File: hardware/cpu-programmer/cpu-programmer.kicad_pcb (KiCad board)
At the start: 2 copper layers, 58 x 22 mm, 13 parts, among them J1 Conn_01x15_Socket, J2 Conn_01x04_Socket, SW1 SW_Push, SW2 SW_Push

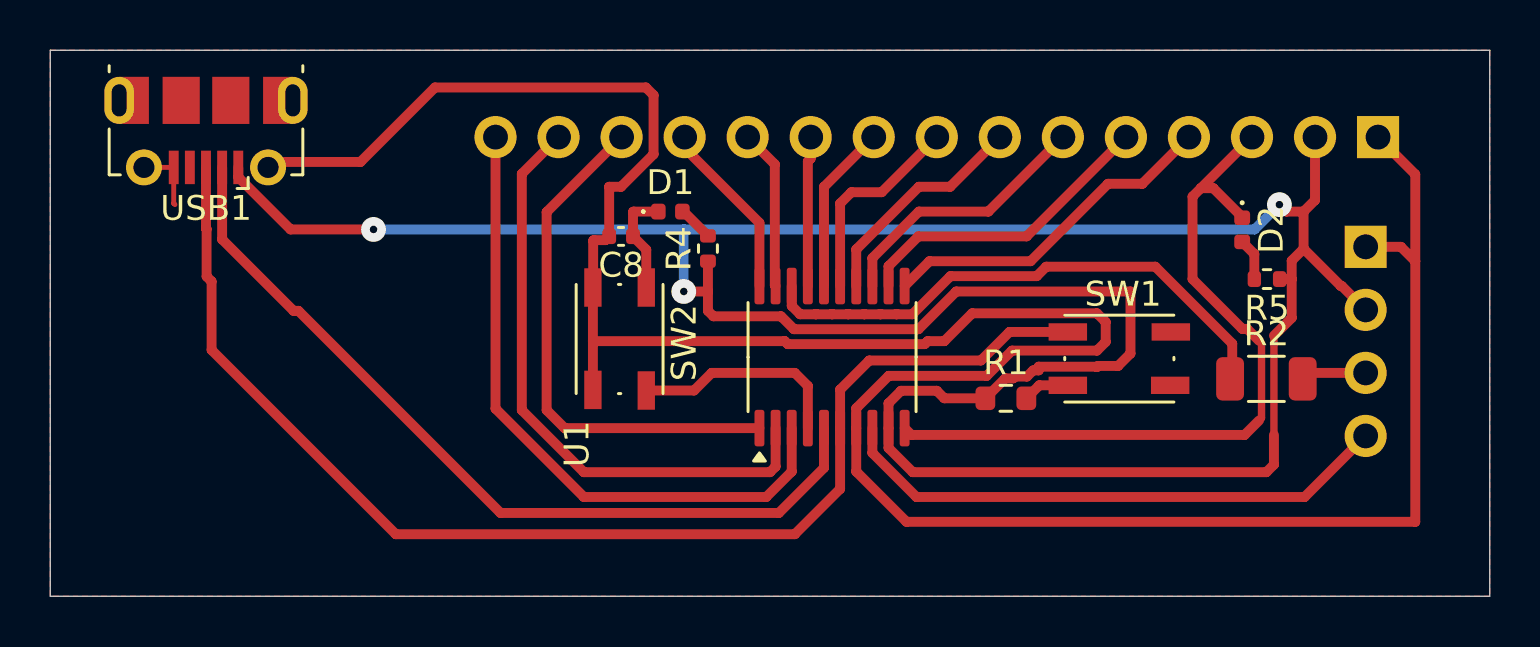
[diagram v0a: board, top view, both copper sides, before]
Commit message: Updated PCB, parts use at least package 0603
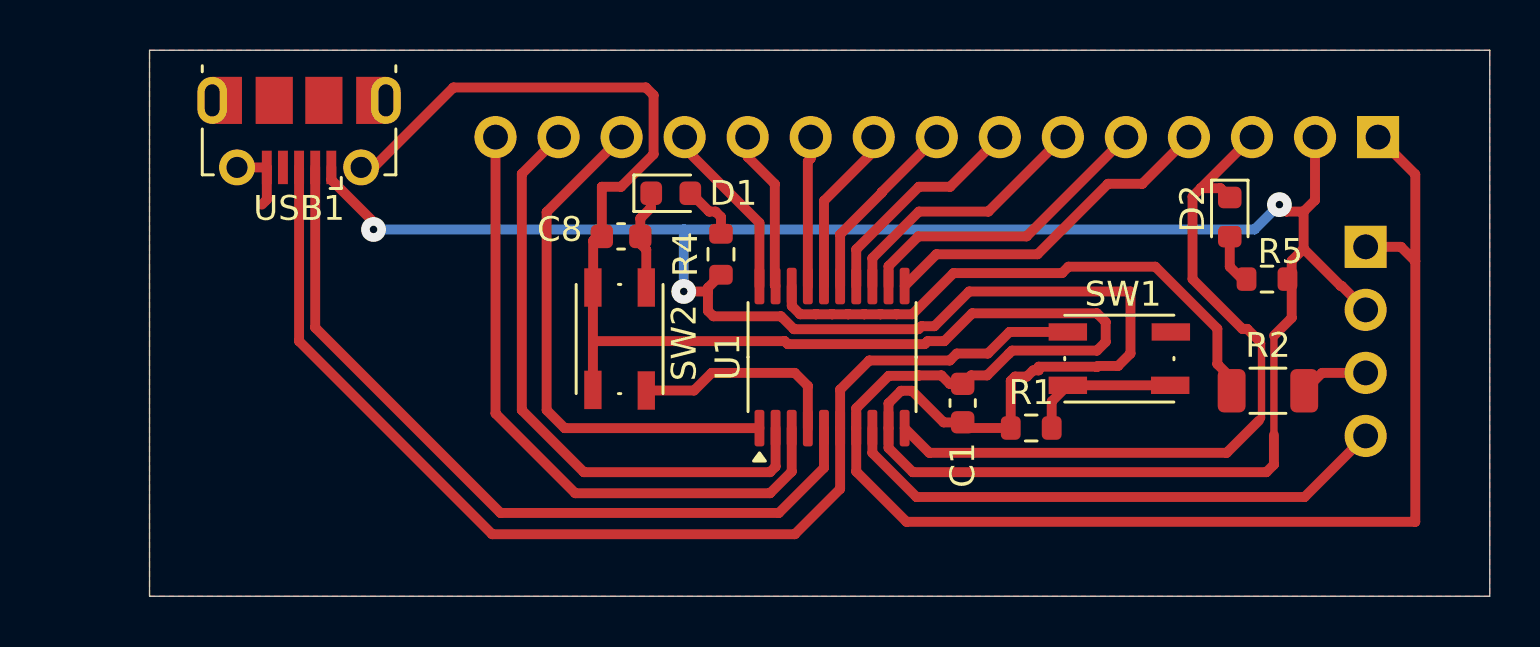
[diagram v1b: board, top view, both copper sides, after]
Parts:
- added C1: 1uF, Capacitor_SMD:C_0603_1608Metric, F.Cu at (49.7, 27.5)
- C8: value 1uF -> 0.1uF; footprint Capacitor_SMD:C_0402_1005Metric -> Capacitor_SMD:C_0603_1608Metric
- D1, D2: footprint LED_SMD:LED_0402_1005Metric -> LED_SMD:LED_0603_1608Metric
- R4, R5: footprint Resistor_SMD:R_0402_1005Metric -> Resistor_SMD:R_0603_1608Metric
- SW1: value SW_Push -> Boot
- SW2: value SW_Push -> Program
- U1: value ~ -> CH32X033F8P6
- moved USB1 3.75 mm to (23.0, 16.5)
- moved R1 1.57 mm to (52.5, 28.5)
- moved D1 0.74 mm to (38.0, 19.0)
- moved D2 0.72 mm to (60.5, 20.0)
- moved R4 0.57 mm to (40.0, 21.5)
- moved R2 0.48 mm to (62.0, 27.0)
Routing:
- net Net-(R1-Pad2): track 1.89 -> 6.11 mm
- net DP: track 50.7 -> 46.9 mm
- net GND: track 110.8 -> 108.0 mm
- net VCC: track 117.3 -> 115.3 mm
- net DM: track 34.1 -> 32.4 mm
- net Net-(D1-A): track 1.44 -> 2.31 mm
- net D1: track 8.33 -> 7.61 mm
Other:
- board size 58 x 22 mm -> 54 x 22 mm

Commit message: Added gerber
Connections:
- J2 pad 3: Net-(J2-Pin_3) -> SWCLK
- R2 pad 2: Net-(J2-Pin_3) -> SWCLK
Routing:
- net SWCLK: track 22.7 -> 33.7 mm, vias 0 -> 2
- net Net-(J2-Pin_3): track 2.77 -> 0.00 mm
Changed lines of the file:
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@@
 		(tenting front back)
 		(pcbplotparams
-			(layerselection 0x00000000_00000000_55555555_55555551)
+			(layerselection 0x00000000_00000000_55555555_5755f5ff)
 			(plot_on_all_layers_selection 0x00000000_00000000_00000000_00000000)
 			(disableapertmacros no)
@@
 			(sketchdnponfab yes)
 			(crossoutdnponfab yes)
-			(subtractmaskfromsilk no)
-			(outputformat 4)
-			(mirror yes)
-			(drillshape 1)
+			(subtractmaskfromsilk yes)
+			(outputformat 1)
+			(mirror no)
+			(drillshape 0)
 			(scaleselection 1)
-			(outputdirectory "")
+			(outputdirectory "./CAM")
 		)
 	)
@@
 	(net 21 "SW2")
 	(net 22 "Net-(R1-Pad2)")
-	(net 23 "Net-(J2-Pin_3)")
-	(net 24 "Net-(D1-A)")
-	(net 25 "Net-(D2-A)")
+	(net 23 "Net-(D1-A)")
+	(net 24 "Net-(D2-A)")
 	(footprint "Button4Pin:SW_Push_1P1T_NO_Vertical_4Pins"
 		(layer "F.Cu")
@@
 			(layers "F.Cu" "F.Mask" "F.Paste")
 			(roundrect_rratio 0.25)
-			(net 25 "Net-(D2-A)")
+			(net 24 "Net-(D2-A)")
 			(pintype "passive")
 		)
@@
 			(layers "F.Cu" "F.Mask" "F.Paste")
 			(roundrect_rratio 0.25)
-			(net 25 "Net-(D2-A)")
+			(net 24 "Net-(D2-A)")
 			(pinfunction "A")
 			(pintype "passive")
@@
 			(layers "F.Cu" "F.Mask" "F.Paste")
 			(roundrect_rratio 0.25)
-			(net 24 "Net-(D1-A)")
+			(net 23 "Net-(D1-A)")
 			(pintype "passive")
 		)
@@
 			(layers "F.Cu" "F.Mask" "F.Paste")
 			(roundrect_rratio 0.25)
-			(net 24 "Net-(D1-A)")
+			(net 23 "Net-(D1-A)")
 			(pinfunction "A")
 			(pintype "passive")
@@
 			(layers "F.Cu" "F.Mask" "F.Paste")
 			(roundrect_rratio 0.222222)
-			(net 23 "Net-(J2-Pin_3)")
+			(net 19 "SWCLK")
 			(pintype "passive")
 		)
@@
 			(layers "*.Cu" "*.Mask")
 			(remove_unused_layers no)
-			(net 23 "Net-(J2-Pin_3)")
+			(net 19 "SWCLK")
 			(pinfunction "Pin_3")
 			(pintype "passive")
@@
 	)
 	(segment
+		(start 63.5 27)
+		(end 63.5 29)
+		(width 0.4)
+		(layer "F.Cu")
+		(net 19)
+	)
+	(segment
 		(start 46.410292 23.9185)
 		(end 45.789708 23.9185)
@@
 	)
 	(segment
+		(start 63.5 27)
+		(end 64.22 26.28)
+		(width 0.4)
+		(layer "F.Cu")
+		(net 19)
+	)
+	(segment
+		(start 64.22 26.28)
+		(end 65.975 26.28)
+		(width 0.4)
+		(layer "F.Cu")
+		(net 19)
+	)
+	(segment
 		(start 43.825 23.903792)
 		(end 43.810292 23.9185)
@@
 	)
 	(segment
+		(start 59.5 28.075)
+		(end 60.575 27)
+		(width 0.4)
+		(layer "F.Cu")
+		(net 19)
+	)
+	(segment
+		(start 59.5 28.5)
+		(end 59.5 28.075)
+		(width 0.4)
+		(layer "F.Cu")
+		(net 19)
+	)
+	(segment
 		(start 44.489708 23.9185)
 		(end 44.475 23.903792)
@@
 		(net 19)
 	)
+	(via
+		(at 63.5 29)
+		(size 1)
+		(drill 0.3)
+		(layers "F.Cu" "B.Cu")
+		(net 19)
+	)
+	(via
+		(at 59.5 28.5)
+		(size 1)
+		(drill 0.3)
+		(layers "F.Cu" "B.Cu")
+		(net 19)
+	)
+	(segment
+		(start 63.5 29)
+		(end 60 29)
+		(width 0.4)
+		(layer "B.Cu")
+		(net 19)
+	)
+	(segment
+		(start 60 29)
+		(end 59.5 28.5)
+		(width 0.4)
+		(layer "B.Cu")
+		(net 19)
+	)
 	(segment
 		(start 46.1 29.503734)
@@
 	)
 	(segment
-		(start 63.5 27)
-		(end 64.22 26.28)
-		(width 0.4)
-		(layer "F.Cu")
-		(net 23)
-	)
-	(segment
-		(start 64.22 26.28)
-		(end 65.975 26.28)
-		(width 0.4)
-		(layer "F.Cu")
-		(net 23)
-	)
-	(segment
 		(start 40 20)
 		(end 40 20.675)
 		(width 0.4)
 		(layer "F.Cu")
-		(net 24)
+		(net 23)
 	)
 	(segment
@@
 		(width 0.4)
 		(layer "F.Cu")
-		(net 24)
+		(net 23)
 	)
 	(segment
@@
 		(width 0.4)
 		(layer "F.Cu")
-		(net 24)
+		(net 23)
 	)
 	(segment
@@
 		(width 0.4)
 		(layer "F.Cu")
-		(net 24)
+		(net 23)
 	)
 	(segment
@@
 		(width 0.4)
 		(layer "F.Cu")
-		(net 24)
+		(net 23)
 	)
 	(segment
@@
 		(width 0.4)
 		(layer "F.Cu")
-		(net 25)
+		(net 24)
 	)
 	(segment
@@
 		(width 0.4)
 		(layer "F.Cu")
-		(net 25)
+		(net 24)
 	)
 	(segment
@@
 		(width 0.4)
 		(layer "F.Cu")
-		(net 25)
+		(net 24)
 	)
 	(zone

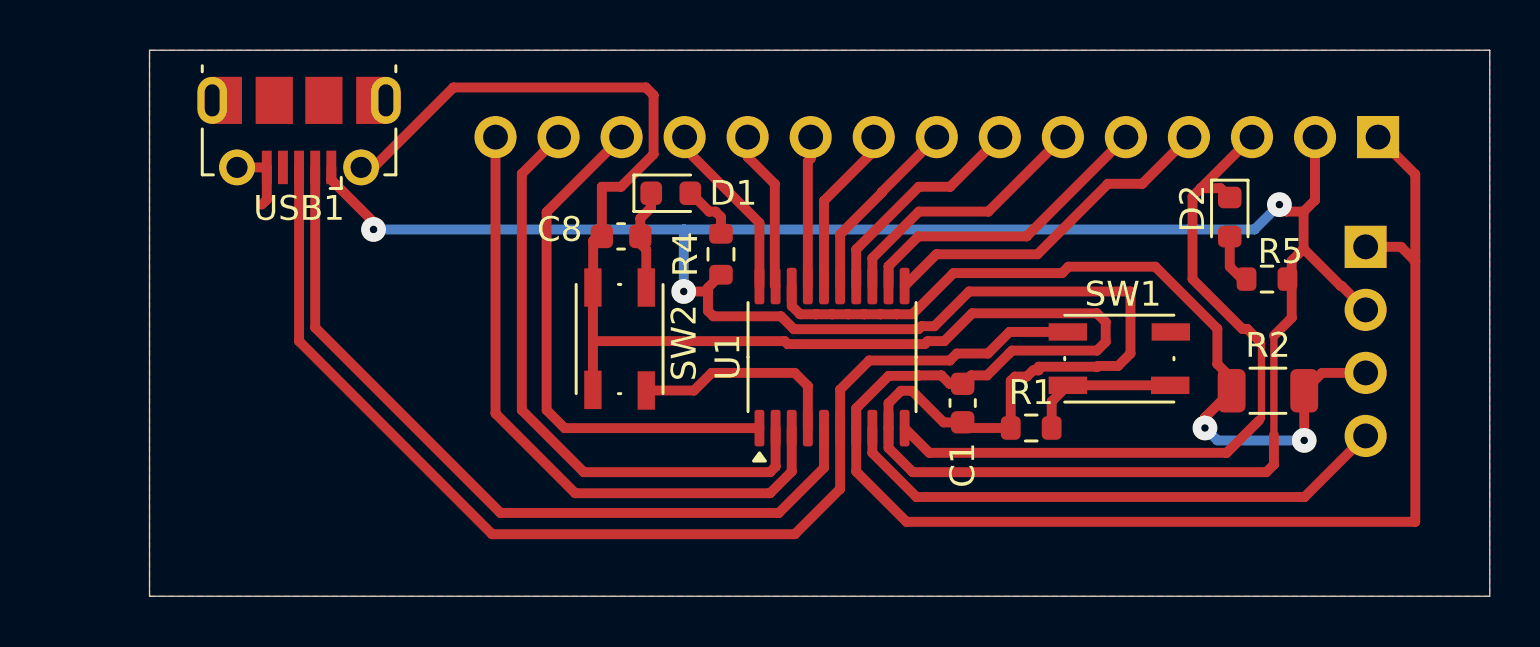
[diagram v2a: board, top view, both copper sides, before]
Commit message: Updated PCB
Fixed silkscreen lables
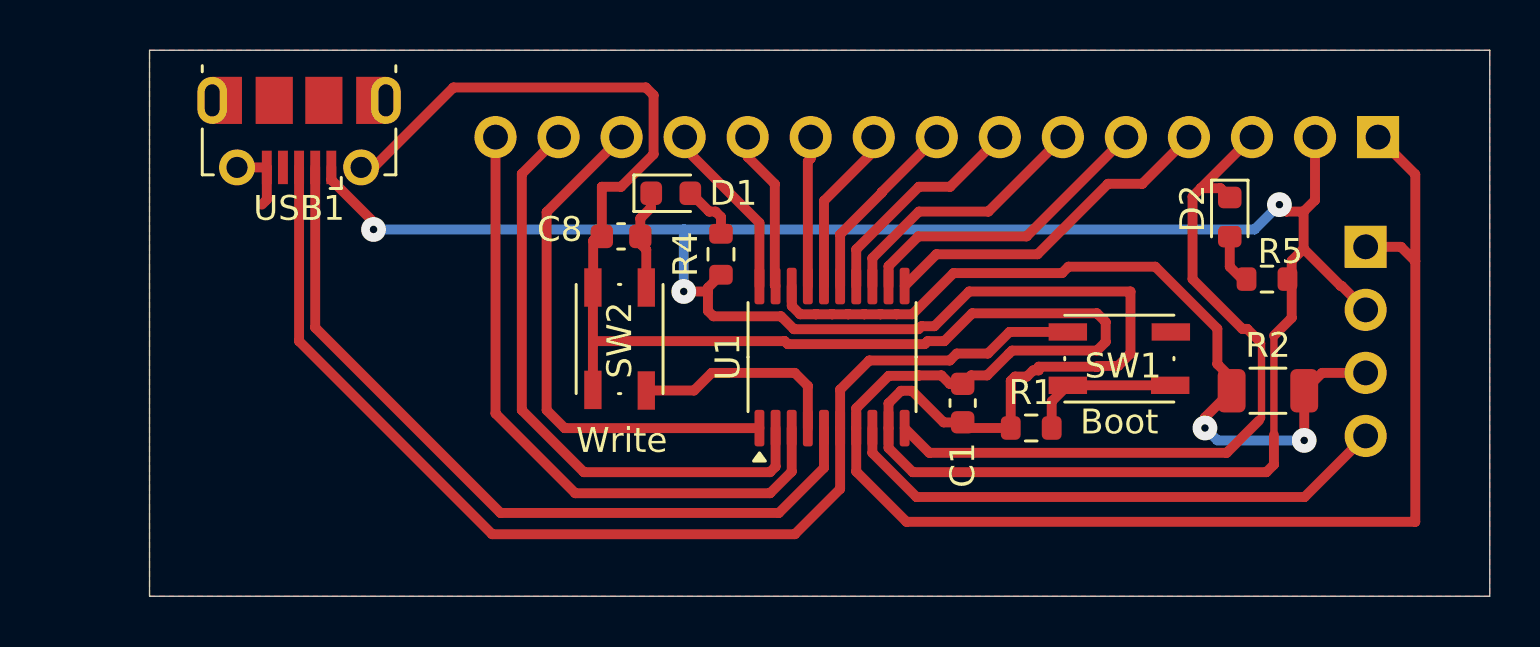
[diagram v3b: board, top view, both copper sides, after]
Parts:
- SW2: value Program -> Write
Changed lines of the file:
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@@
 		(tags "tactile switch Wurth Wuerth")
 		(property "Reference" "SW1"
-			(at 0.15 -2.6 0)
+			(at 0.15 0.295 0)
 			(layer "F.SilkS")
 			(effects
@@
 		(property "Value" "Boot"
 			(at 0 2.55 0)
-			(layer "F.Fab")
+			(layer "F.SilkS")
 			(effects
 				(font
@@
 			(at 0.15 -2.6 90)
 			(layer "F.SilkS")
+			(hide yes)
 			(effects
 				(font
@@
 			)
 		)
-		(property "Value" "Program"
-			(at 0 2.55 90)
-			(layer "F.Fab")
+		(property "Value" "Write"
+			(at 4.085762 -0.085147 0)
+			(layer "F.SilkS")
 			(effects
 				(font
@@
 		(fp_text user "${REFERENCE}"
 			(at 0.05 0 90)
-			(layer "F.Fab")
-			(effects
-				(font
+			(layer "F.SilkS")
+			(effects
+				(font

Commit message: Fixed differential pair
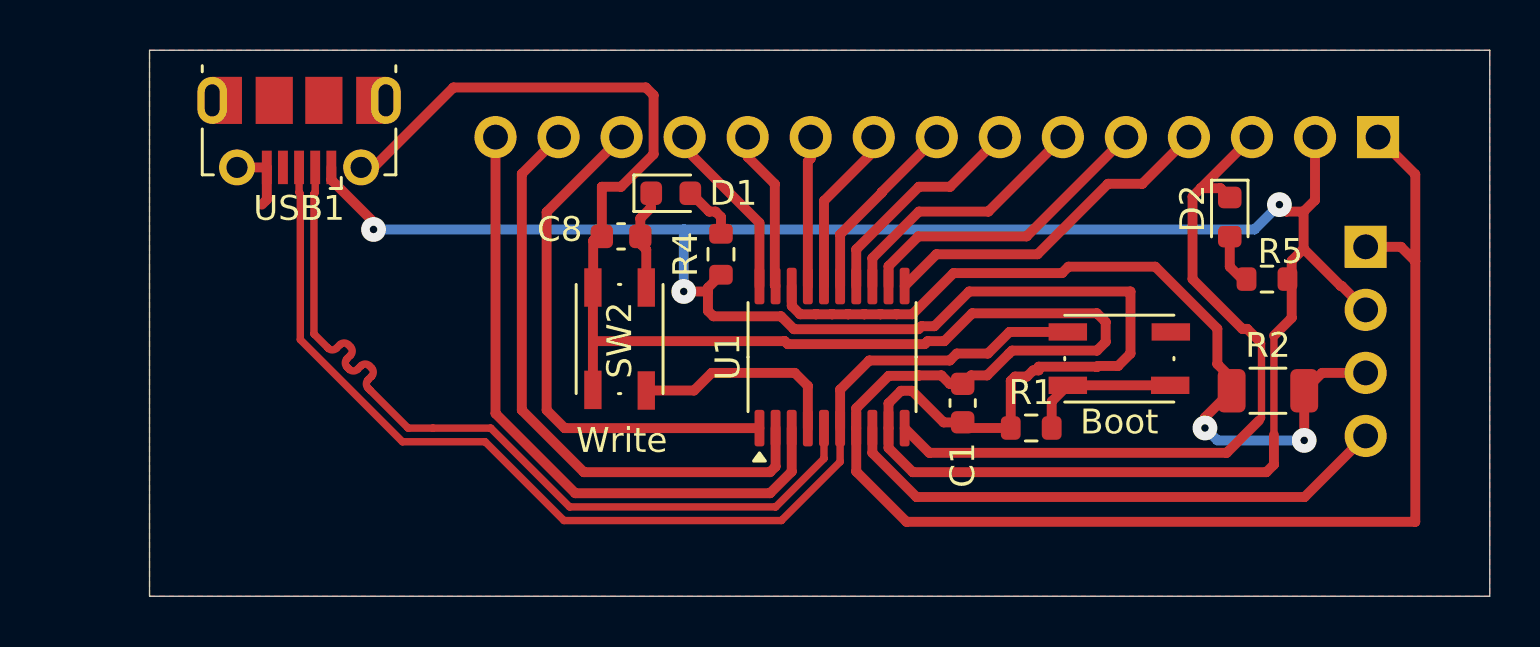
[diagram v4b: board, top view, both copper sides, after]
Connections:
- net DM renamed D-
- net DP renamed D+
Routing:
- net D-: track 32.4 -> 34.0 mm
- net D+: track 46.9 -> 45.8 mm
